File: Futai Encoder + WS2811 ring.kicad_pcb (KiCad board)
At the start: 2 copper layers, 31.1 x 49 mm, 52 parts, among them J1 Conn_02x05_Top_Bottom, SW1 RotaryEncoder_Switch_RGB

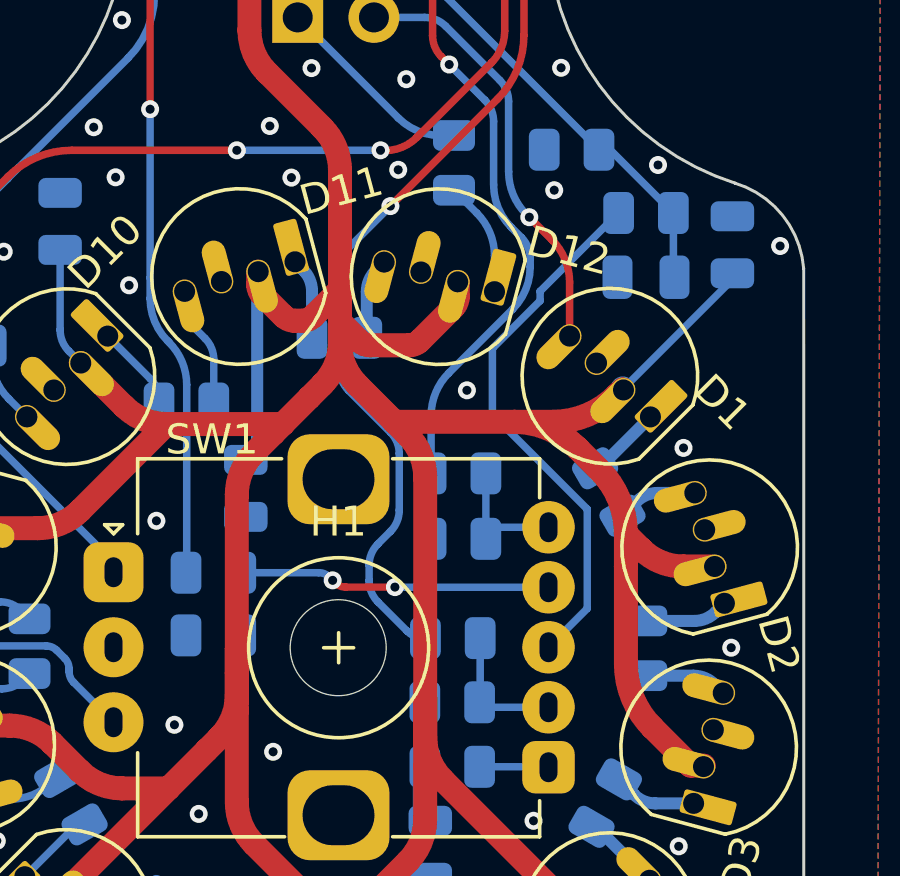
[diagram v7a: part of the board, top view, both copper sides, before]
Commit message: smaller center hole
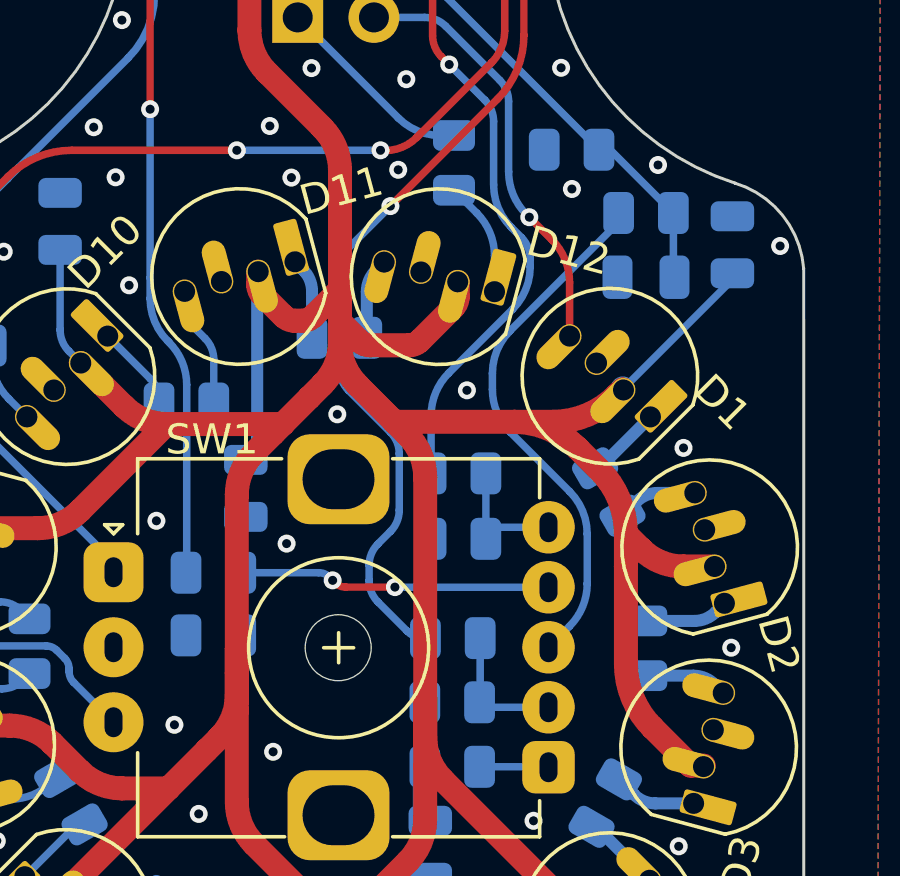
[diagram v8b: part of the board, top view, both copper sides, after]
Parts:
- H1: footprint andilge KiCad footprints:MountingHole_3.2mm_M3 -> andilge KiCad footprints:MountingHole_2.2mm_M2
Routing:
- net SWC: track 18.2 -> 17.7 mm
- net GND: vias 39 -> 41
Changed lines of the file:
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@@
     )
   )
-  (footprint "andilge KiCad footprints:MountingHole_3.2mm_M3" (layer "F.Cu")
+  (footprint "andilge KiCad footprints:MountingHole_2.2mm_M2" (layer "F.Cu")
     (at 135.04 86.24)
-    (descr "Mounting Hole 3.2mm, no annular, M3")
-    (tags "mounting hole 3.2mm no annular m3")
-    (property "Sheetfile" "Futai Encoder + WS2811 ring.kicad_sch")
-    (property "Sheetname" "")
-    (attr exclude_from_pos_files exclude_from_bom)
-    (fp_text reference "H1" (at 0 -4.2) (layer "F.SilkS")
+    (descr "Mounting Hole 2.2mm, no annular, M2")
+    (tags "mounting hole 2.2mm no annular m2")
+    (property "Sheetfile" "Futai Encoder + WS2811 ring.kicad_sch")
+    (property "Sheetname" "")
+    (attr exclude_from_pos_files)
+    (fp_text reference "H1" (at 0 -3.2) (layer "F.SilkS") hide
       (effects (font (size 1 1) (thickness 0.15)))
     )
-    (fp_text value "MountingHole" (at 0 4.2) (layer "F.Fab")
+    (fp_text value "MountingHole" (at 0 3.2) (layer "F.Fab")
       (effects (font (size 1 1) (thickness 0.15)))
     )
@@
       (effects (font (size 1 1) (thickness 0.15)))
     )
-    (fp_circle (center 0 0) (end 3.2 0) (layer "Cmts.User") (width 0.15) (fill none))
-    (fp_circle (center 0 0) (end 3.45 0) (layer "F.CrtYd") (width 0.05) (fill none))
-    (pad "" np_thru_hole circle locked (at 0 0) (size 3.2 3.2) (drill 3.2) (layers *.Cu *.Mask))
+    (fp_circle (center 0 0) (end 2.2 0) (layer "Cmts.User") (width 0.15) (fill none))
+    (fp_circle (center 0 0) (end 2.45 0) (layer "F.CrtYd") (width 0.05) (fill none))
+    (pad "" np_thru_hole circle locked (at 0 0) (size 2.2 2.2) (drill 2.2) (layers *.Cu *.Mask))
   )
   (footprint "andilge KiCad footprints:WS2811D-F5-1261" (layer "F.Cu")
@@
   (via (at 128.98 82.01) (size 0.6) (drill 0.3) (layers "F.Cu" "B.Cu") (free) (net 1))
   (via (at 141.6 97.68) (size 0.6) (drill 0.3) (layers "F.Cu" "B.Cu") (free) (net 1))
-  (via (at 142.24 70.99) (size 0.6) (drill 0.3) (layers "F.Cu" "B.Cu") (free) (net 1))
+  (via (at 142.83 70.95) (size 0.6) (drill 0.3) (layers "F.Cu" "B.Cu") (free) (net 1))
   (via (at 146.39 92.86) (size 0.6) (drill 0.3) (layers "F.Cu" "B.Cu") (free) (net 1))
+  (via (at 133.32 82.77) (size 0.6) (drill 0.3) (layers "F.Cu" "B.Cu") (free) (net 1))
   (via (at 131.16 63.5) (size 0.6) (drill 0.3) (layers "F.Cu" "B.Cu") (free) (net 1))
   (via (at 141.55 92.01) (size 0.6) (drill 0.3) (layers "F.Cu" "B.Cu") (free) (net 1))
@@
   (via (at 129.82 54.18) (size 0.6) (drill 0.3) (layers "F.Cu" "B.Cu") (free) (net 1))
   (via (at 120.86 86.15) (size 0.6) (drill 0.3) (layers "F.Cu" "B.Cu") (free) (net 1))
+  (via (at 135.01 78.46) (size 0.6) (drill 0.3) (layers "F.Cu" "B.Cu") (free) (net 1))
   (segment (start 135.788427 63.96) (end 137.224073 63.96) (width 0.25) (layer "B.Cu") (net 2))
   (segment (start 143.7325 69.64) (end 144.1025 69.64) (width 0.25) (layer "B.Cu") (net 2))
@@
   (segment (start 131.7925 83.74) (end 134.392893 83.74) (width 0.25) (layer "B.Cu") (net 19))
   (arc (start 134.746447 83.886447) (mid 134.584235 83.77806) (end 134.392893 83.74) (width 0.25) (layer "B.Cu") (net 19))
-  (segment (start 144.38 71.75) (end 141.77 74.36) (width 0.25) (layer "B.Cu") (net 20))
-  (segment (start 143.34 81.62) (end 143.34 84.935) (width 0.25) (layer "B.Cu") (net 20))
-  (segment (start 141.77 74.36) (end 141.77 74.675718) (width 0.25) (layer "B.Cu") (net 20))
-  (segment (start 144.23 71.75) (end 144.3875 71.75) (width 0.25) (layer "B.Cu") (net 20))
-  (segment (start 140.18 78.46) (end 143.34 81.62) (width 0.25) (layer "B.Cu") (net 20))
-  (segment (start 144.3875 71.75) (end 144.38 71.75) (width 0.25) (layer "B.Cu") (net 20))
-  (segment (start 141.77 74.675718) (end 140.18 76.265718) (width 0.25) (layer "B.Cu") (net 20))
-  (segment (start 143.34 84.935) (end 142.05 86.225) (width 0.25) (layer "B.Cu") (net 20))
-  (segment (start 140.18 76.265718) (end 140.18 78.46) (width 0.25) (layer "B.Cu") (net 20))
+  (segment (start 140.18 77.094145) (end 140.18 77.631573) (width 0.25) (layer "B.Cu") (net 20))
+  (segment (start 142.754213 85.520787) (end 142.05 86.225) (width 0.25) (layer "B.Cu") (net 20))
+  (segment (start 144.3875 72.058218) (end 140.765786 75.679932) (width 0.25) (layer "B.Cu") (net 20))
+  (segment (start 143.34 82.448427) (end 143.34 84.106573) (width 0.25) (layer "B.Cu") (net 20))
+  (segment (start 140.765787 79.045787) (end 142.754214 81.034214) (width 0.25) (layer "B.Cu") (net 20))
+  (segment (start 144.3875 71.75) (end 144.3875 72.058218) (width 0.25) (layer "B.Cu") (net 20))
+  (arc (start 140.18 77.094145) (mid 140.332241 76.328778) (end 140.765786 75.679932) (width 0.25) (layer "B.Cu") (net 20))
+  (arc (start 140.765787 79.045787) (mid 140.332241 78.39694) (end 140.18 77.631573) (width 0.25) (layer "B.Cu") (net 20))
+  (arc (start 143.34 84.106573) (mid 143.187759 84.87194) (end 142.754213 85.520787) (width 0.25) (layer "B.Cu") (net 20))
+  (arc (start 142.754214 81.034214) (mid 143.187759 81.68306) (end 143.34 82.448427) (width 0.25) (layer "B.Cu") (net 20))
   (segment (start 127.55 83.39) (end 127.55 83.725) (width 0.25) (layer "B.Cu") (net 21))
   (segment (start 124.028679 70.601321) (end 123.438679 71.191321) (width 0.25) (layer "B.Cu") (net 21))
